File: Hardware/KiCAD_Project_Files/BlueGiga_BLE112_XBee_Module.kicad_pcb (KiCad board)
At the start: 4 copper layers, 24.5 x 24.4 mm, 11 parts, among them J2 HEADER_F_XBEE_PTH, P1 HEADER_2X5, U1 BLE112-A, U2 AAT3221

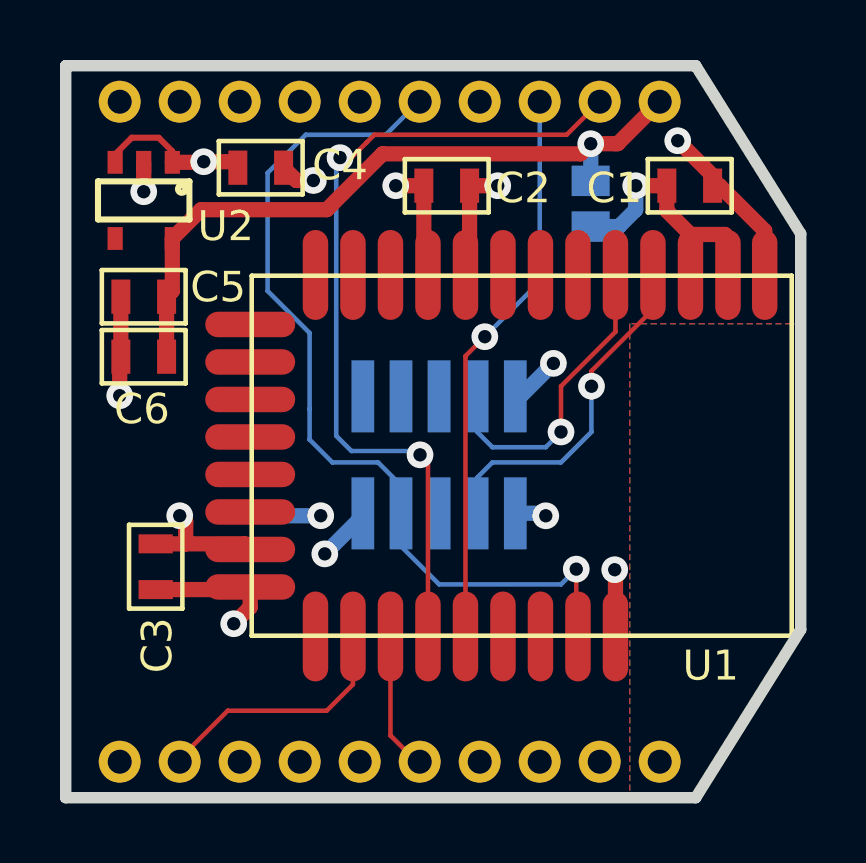
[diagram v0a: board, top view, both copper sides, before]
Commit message: Corrected voltage regulator connections and added level shifters to inputs to BLE112.
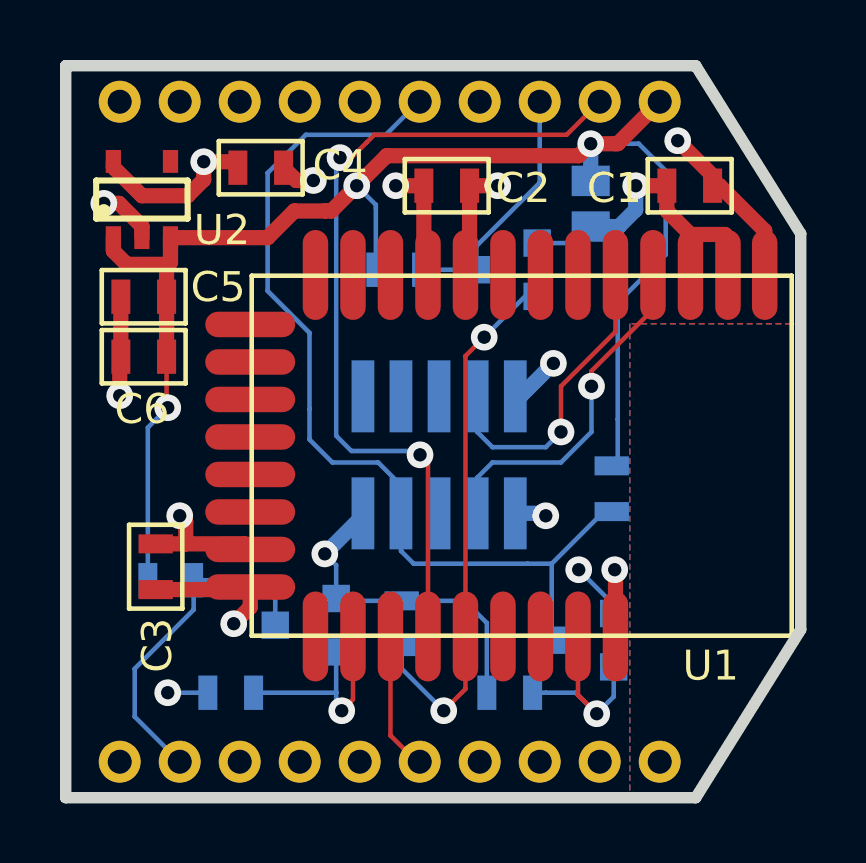
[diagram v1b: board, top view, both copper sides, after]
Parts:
- added Q1: BSS138, Active:SOT-23-3_GDS, B.Cu at (116.2, 99.8)
- added Q2: BSS138, Active:SOT-23-3_GDS, B.Cu at (113.7, 87.4)
- added Q3: BSS138, Active:SOT-23-3_GDS, B.Cu at (107.0, 99.2)
- added R1: 10k, Passive:0603, B.Cu at (113.8, 101.5)
- added R2: 10k, Passive:0603, B.Cu at (110.2, 99.2)
- added R3: 10k, Passive:0603, B.Cu at (104.5, 101.5)
- added R4: 10k, Passive:0603, B.Cu at (117.2, 94.7)
- added R5: 10k, Passive:0603, B.Cu at (110.1, 87.4)
- added R6: 10k, Passive:0603, B.Cu at (102.5, 97.8)
- P1: renamed from J2; value HEADER_F_XBEE_PTH -> XBEE HEADER
- P2: renamed from P1; value HEADER_2X5 -> DEBUG
- moved U2 0.07 mm to (101.5, 85.1), turned to 90 degrees
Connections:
- C1 pad 1: +3.3V -> +3V3
- C2 pad 1: +3.3V -> +3V3
- C3 pad 1: +3.3V -> +3V3
- C4 pad 1: +3.3V -> +3V3
- C5 pad 1: VCC -> VDD
- C6 pad 1: VCC -> VDD
- LK1 pad 1: +3.3V -> +3V3
- LK1 pad 2: VCC -> VDD
- P1 pad 1: VCC -> VDD
- P1 pad 11: (no net) -> Net-(P1-Pad11)
- P1 pad 13: (no net) -> Net-(P1-Pad13)
- P1 pad 14: (no net) -> Net-(P1-Pad14)
- P1 pad 15: (no net) -> Net-(P1-Pad15)
- P1 pad 17: (no net) -> Net-(P1-Pad17)
- P1 pad 18: (no net) -> Net-(P1-Pad18)
- P1 pad 19: (no net) -> Net-(P1-Pad19)
- P1 pad 20: (no net) -> Net-(P1-Pad20)
- P1 pad 4: (no net) -> Net-(P1-Pad4)
- P1 pad 6: (no net) -> Net-(P1-Pad6)
- P1 pad 7: (no net) -> Net-(P1-Pad7)
- P1 pad 8: (no net) -> Net-(P1-Pad8)
- P1 pad 9: (no net) -> Net-(P1-Pad9)
- P2 pad 10: (no net) -> Net-(P2-Pad10)
- P2 pad 2: +3.3V -> +3V3
- P2 pad 5: (no net) -> Net-(P2-Pad5)
- P2 pad 6: (no net) -> Net-(P2-Pad6)
- P2 pad 8: (no net) -> Net-(P2-Pad8)
- P2 pad 9: +3.3V -> +3V3
- U1 pad 11: (no net) -> Net-(U1-Pad11)
- U1 pad 12: (no net) -> Net-(U1-Pad12)
- U1 pad 13: (no net) -> Net-(U1-Pad13)
- U1 pad 14: (no net) -> Net-(U1-Pad14)
- U1 pad 15: (no net) -> Net-(U1-Pad15)
- U1 pad 16: (no net) -> Net-(U1-Pad16)
- U1 pad 17: (no net) -> Net-(U1-Pad17)
- U1 pad 18: (no net) -> Net-(U1-Pad18)
- U1 pad 19: (no net) -> Net-(U1-Pad19)
- U1 pad 2: +3.3V -> +3V3
- U1 pad 20: +3.3V -> +3V3
- U1 pad 22: (no net) -> Net-(U1-Pad22)
- U1 pad 23: RT -> RT_3V3
- U1 pad 26: RX -> RX_3V3
- U1 pad 27: (no net) -> Net-(U1-Pad27)
- U1 pad 28: (no net) -> Net-(U1-Pad28)
- U1 pad 29: RESET -> RESET_3V3
- U1 pad 3: +3.3V -> +3V3
- U1 pad 6: (no net) -> Net-(U1-Pad6)
- U1 pad 7: (no net) -> Net-(U1-Pad7)
- U1 pad 8: (no net) -> Net-(U1-Pad8)
- U1 pad 9: +3.3V -> +3V3
- U2 pad 1: +3.3V -> VDD
- U2 pad 3: +3.3V -> VDD
- U2 pad 4: (no net) -> Net-(U2-Pad4)
- U2 pad 5: VCC -> +3V3
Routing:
- net VDD: track 0.00 -> 50.2 mm, vias 0 -> 3
- net +3V3: track 0.00 -> 44.5 mm, vias 0 -> 8
- net +3.3V: track 29.2 -> 0.00 mm, vias 6 -> 0
- net VCC: track 23.4 -> 0.00 mm, vias 1 -> 0
- net RX_3V3: track 0.00 -> 18.1 mm, vias 0 -> 2
- net RX: track 18.9 -> 8.30 mm, vias 1 -> 0
- net RT_3V3: track 0.00 -> 7.45 mm, vias 0 -> 1
- net RESET_3V3: track 0.00 -> 7.14 mm, vias 0 -> 1
- net RT: track 8.50 -> 11.4 mm
- net RESET: track 30.1 -> 33.0 mm, vias 1 -> 0
- net (no net): track 1.20 -> 0.00 mm, vias 1 -> 0
- net GND: track 23.2 -> 24.2 mm
- added copper zone on Inner2-Pwr.Cu, net +3V3
- removed copper zone on Inner2-Pwr.Cu, net +3.3V
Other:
- board text added: "REV 3"
- board text removed: "REV 2"
